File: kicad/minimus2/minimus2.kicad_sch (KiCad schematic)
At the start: 68 parts, among them J1 PROG_SER, J2 LM, J3 LM, Q1 RSE, Q2 RFE, Q3 LFE, Q4 LSE, Q5 DMN3051L, SW1 RESET, SW2 USER_A, SW3 USER_B, U1 LSM6DSRTR, U2 STM32U575CITx, U3 DRV8835, U4 AS5047D, U5 AS5047D

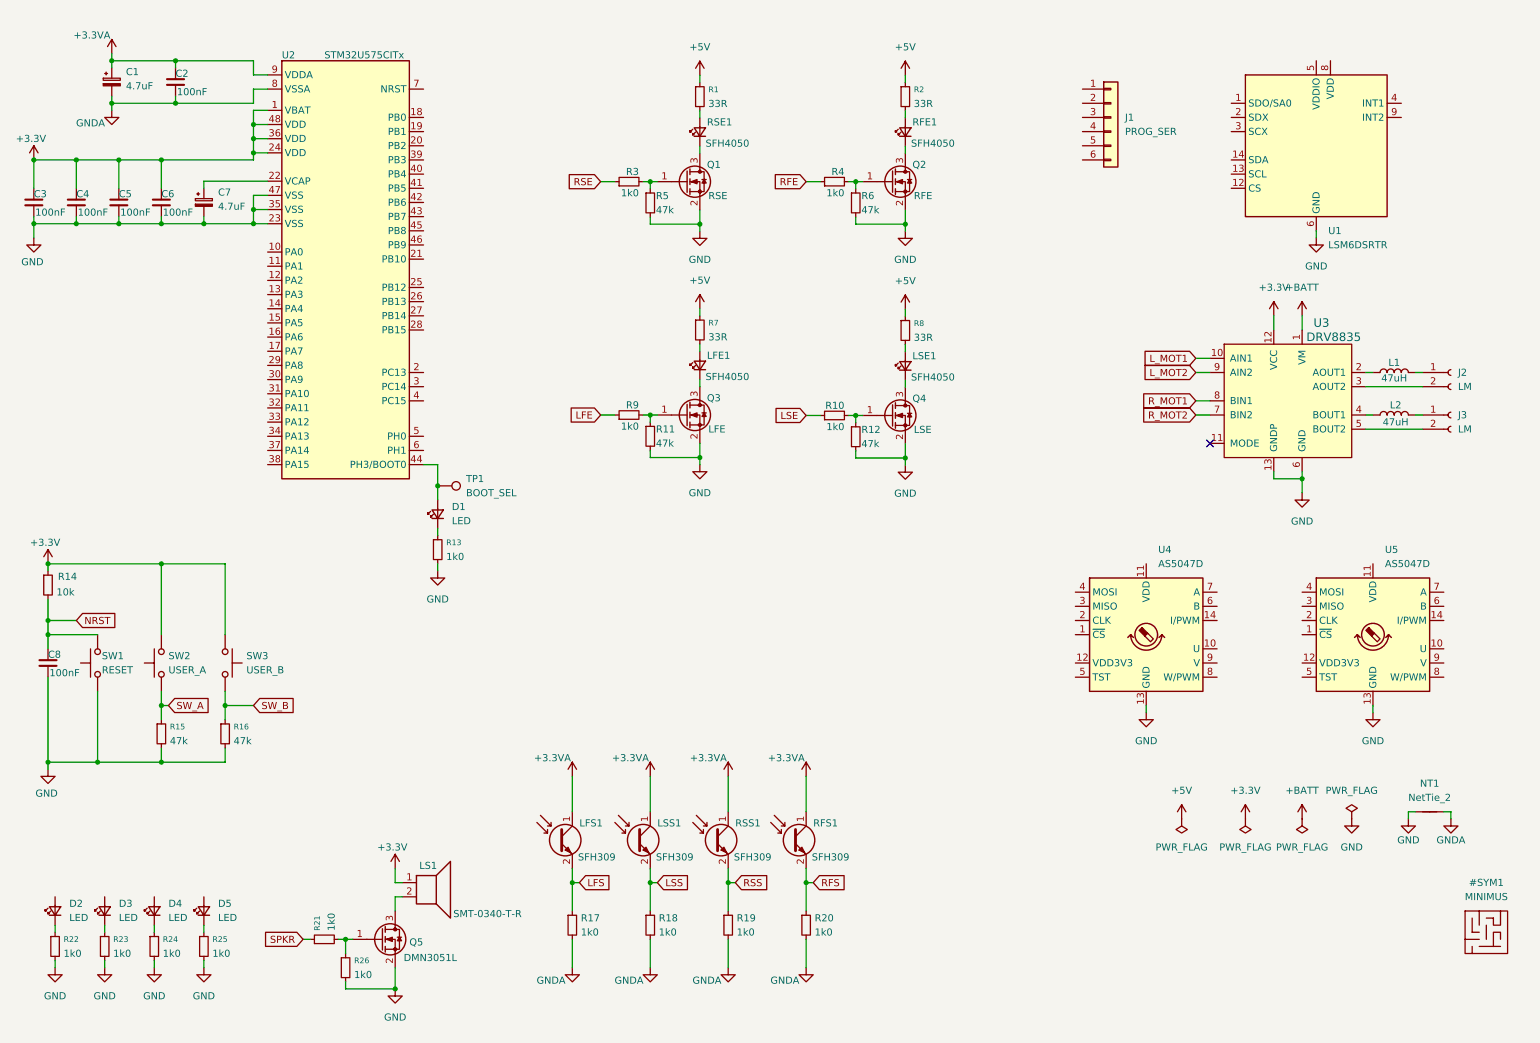
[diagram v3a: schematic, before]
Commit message: add some parts libraries
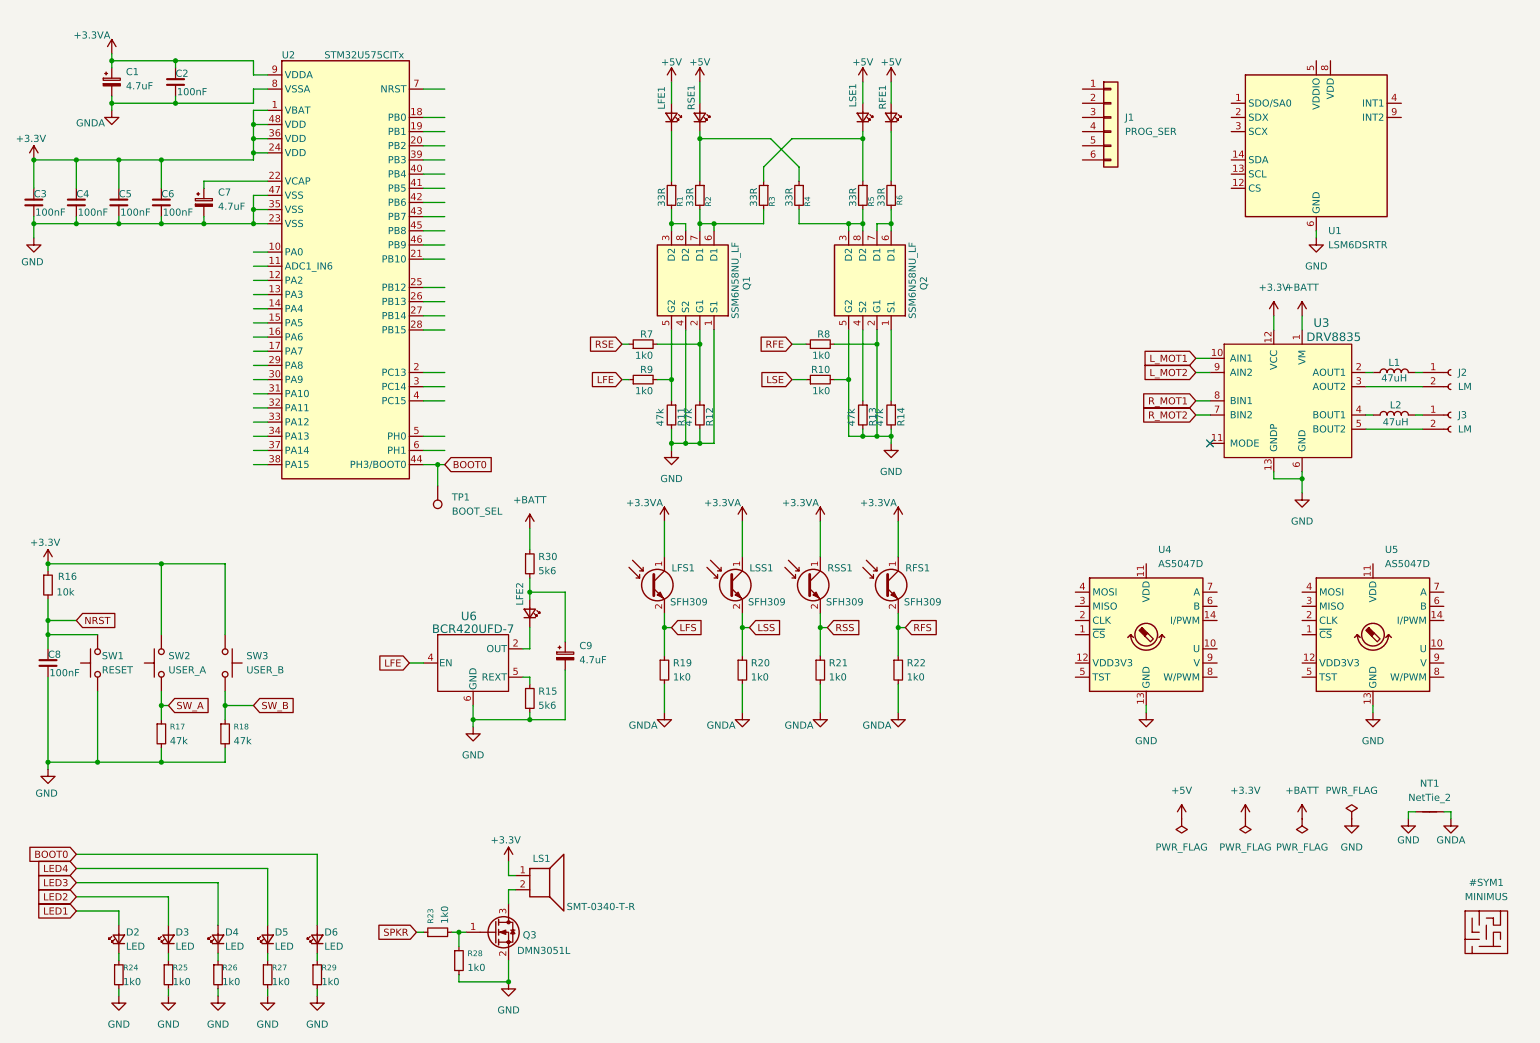
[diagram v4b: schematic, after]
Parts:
- removed D1: LED, LED_SMD:LED_0402_1005Metric, symbol Device:LED_Small
- removed Q1: RSE, Package_TO_SOT_SMD:SOT-23, symbol Transistor_FET:DMN3051L
- removed Q2: RFE, Package_TO_SOT_SMD:SOT-23, symbol Transistor_FET:DMN3051L
- removed Q3: LFE, Package_TO_SOT_SMD:SOT-23, symbol Transistor_FET:DMN3051L
- removed Q4: LSE, Package_TO_SOT_SMD:SOT-23, symbol Transistor_FET:DMN3051L
- removed R5, R6: 47k, Resistor_SMD:R_0402_1005Metric, symbol Device:R_Small
- added C9: 4.7uF, Capacitor_SMD:C_0805_2012Metric, symbol Device:C_Polarized_Small
- added D6: LED, LED_SMD:LED_0402_1005Metric, symbol Device:LED_Small
- added LFE2: SFH4050, LED_THT:LED_D3.0mm_Horizontal_O1.27mm_Z2.0mm_IRBlack, symbol Device:LED_Small
- added Q1, Q2: SSM6N58NU_LF, SSM6N58NU_LF:SON65P200X200X80-8N, symbol minimus:SSM6N58NU_LF_BLOCK
- added R1, R2: 33R, Resistor_SMD:R_0402_1005Metric, symbol Device:R_Small
- added R14: 47k, Resistor_SMD:R_0402_1005Metric, symbol Device:R_Small
- added R15, R30: 5k6, Resistor_SMD:R_0402_1005Metric, symbol Device:R_Small
- added R29: 1k0, Resistor_SMD:R_0402_1005Metric, symbol Device:R_Small
- added U6: BCR420UFD-7, U-DFN2020-6_2X2_DIO, symbol BCR420UFD:BCR420UFD-7
- R13: value 1k0 -> 47k
- R3, R4: value 1k0 -> 33R
- R7, R8: value 33R -> 1k0
- renumbered RSE1 to LSE1, Q5 to Q3, R14 to R16, R15 to R17, R16 to R18, R17 to R19, R18 to R20, R19 to R21, R20 to R22, R21 to R23, R22 to R24, R23 to R25, R24 to R26, R25 to R27, R26 to R28, R1 to R5, R2 to R6, LSE1 to RSE1
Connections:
- net +5V: now also LFE1.2 (A), LSE1.2 (A), RFE1.2 (A), RSE1.2 (A); no longer R5.1, R6.1, R7.1, R8.1
- net +BATT: now also R30.1
- net GND: now also R10.2, R8.2, C9.2, Q1.1 (S1), Q1.4 (S2), Q2.2 (G1), Q2.5 (G2), R14.2, R15.2, R29.2, U6.6 (GND)
- net LFE: now also U6.4 (EN), U6.7 (OUT)
- net RFE: now also R8.1; no longer R4.1
- net RSE: now also R7.1; no longer R3.1
- net LED1: now reaches D2.2 (A)
- net at R5.2: now also R4.2, Q2.3 (D2), Q2.8 (D2); no longer LSE1.2 (A)
- net at RSE1.1 (K): now also R4.1, R2.1
- net at R13.1: now also Q2.4 (S2)
- net LED2: now reaches D3.2 (A)
- net at R11.1, R9.2: now also Q1.5 (G2)
- net at LFE1.1 (K): now also R1.1
- net at R3.2: now also Q1.6 (D1), Q1.7 (D1), R2.2
- net at LSE1.1 (K): now also R3.1, R5.1
- net at RFE1.1 (K): now also R6.1
- net at R12.1: now also R7.2, Q1.2 (G1); no longer R10.2
- net BOOT0: now reaches TP1.1, U2.44 (PH3/BOOT0)
- net BOOT0: now also D6.2 (A)
- net LED4: now reaches D5.2 (A)
- net LED3: now reaches D4.2 (A)
- net at R6.2: now also Q2.6 (D1), Q2.7 (D1); no longer RFE1.2 (A)
- new net: Q2.1 (S1), R14.1
- new net: Q1.3 (D2), Q1.8 (D2), R1.2
- new net: C9.1, LFE2.2 (A), R30.2
- new net: LFE2.1 (K), U6.2 (OUT)
- new net: R15.1, U6.5 (REXT)
- new net: D6.1 (K), R29.1
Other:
- moved on the sheet: D2, D3, D4, D5, LFE1, LFS1, LS1, LSE1, LSS1, Q3, R19, R20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

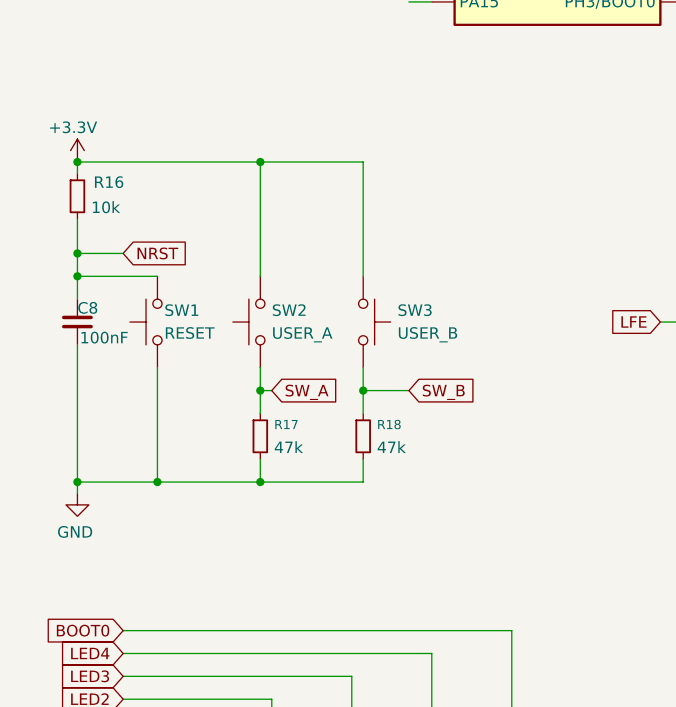
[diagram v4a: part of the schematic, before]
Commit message: add 3D model for BCR420UFD
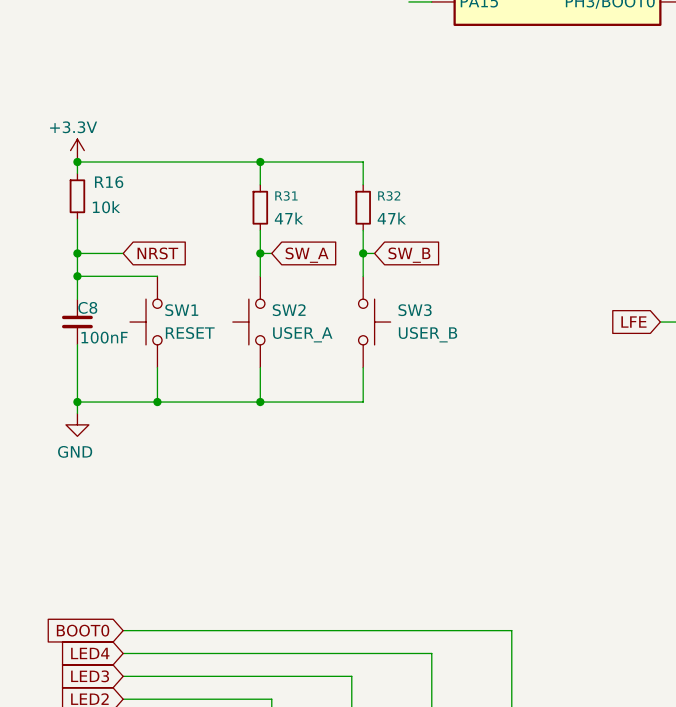
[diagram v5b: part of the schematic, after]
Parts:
- removed R17, R18: 47k, Resistor_SMD:R_0402_1005Metric, symbol Device:R_Small
- added R31, R32: 47k, Resistor_SMD:R_0402_1005Metric, symbol Device:R_Small
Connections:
- net +3.3V: now also R31.1, R32.1; no longer SW2.2, SW3.1
- net GND: now also SW2.1, SW3.2
- net SW_A: now also SW2.2, R31.2; no longer SW2.1
- net SW_B: now also SW3.1, R32.2; no longer SW3.2
